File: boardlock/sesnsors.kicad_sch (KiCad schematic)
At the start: 1 part, among them U1 LSM6DS3

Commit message: update
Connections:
- net +3V3: now reaches U1.5 (VDDIO)
- net +3V3: now also U1.8 (VDD)
- net GND: now reaches U1.6 (GND), U1.7 (GND)
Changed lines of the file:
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@@
 (kicad_sch (version 20230121) (generator eeschema)
   (paper "A4")
+  (junction (at 81.28 44.45) (diameter 0) (color 0 0 0 0)
+  )
+  (wire (pts (xy 81.28 44.45) (xy 83.82 44.45))
+    (stroke (width 0) (type default))
+  )
+  (wire (pts (xy 81.28 81.28) (xy 81.28 86.36))
+    (stroke (width 0) (type default))
+  )
+  (wire (pts (xy 81.28 50.8) (xy 81.28 44.45))
+    (stroke (width 0) (type default))
+  )
+  (wire (pts (xy 83.82 50.8) (xy 83.82 44.45))
+    (stroke (width 0) (type default))
+  )
+  (wire (pts (xy 81.28 44.45) (xy 81.28 39.37))
+    (stroke (width 0) (type default))
+  )
   (symbol (lib_id "Sensor_Motion:LSM6DS3") (at 81.28 66.04 0) (unit 1)
     (in_bom yes) (on_board yes) (dnp no) (fields_autoplaced)
@@
         )
       )
+    )
+  )
+  (symbol (lib_id "power:+3V3") (at 81.28 39.37 0) (unit 1)
+    (in_bom yes) (on_board yes) (dnp no) (fields_autoplaced)
+    (property "Reference" "#PWR01" (at 81.28 43.18 0)
+      (effects (font (size 1.27 1.27)) hide)
+    )
+    (property "Value" "+3V3" (at 81.28 35.2369 0)
+      (effects (font (size 1.27 1.27)))
+    )
+    (property "Footprint" "" (at 81.28 39.37 0)
+      (effects (font (size 1.27 1.27)) hide)
+    )
+    (property "Datasheet" "" (at 81.28 39.37 0)
+      (effects (font (size 1.27 1.27)) hide)
+    )
+    (pin "1")
+    (instances
+      (project "boardlock"
+        (path "/48f24f42-fd64-4860-9f12-ca34cf195758/17b4aebf-aea4-4bb2-a07c-86de8cf47820"
+          (reference "#PWR01") (unit 1)
+        )
+      )
+    )
+  )
+  (symbol (lib_id "power:GND") (at 81.28 86.36 0) (unit 1)
+    (in_bom yes) (on_board yes) (dnp no) (fields_autoplaced)
+    (property "Reference" "#PWR02" (at 81.28 92.71 0)
+      (effects (font (size 1.27 1.27)) hide)
+    )
+    (property "Value" "GND" (at 81.28 90.4931 0)
+      (effects (font (size 1.27 1.27)))
+    )
+    (property "Footprint" "" (at 81.28 86.36 0)
+      (effects (font (size 1.27 1.27)) hide)
+    )
+    (property "Datasheet" "" (at 81.28 86.36 0)
+      (effects (font (size 1.27 1.27)) hide)
+    )
+    (pin "1")
+    (instances
+      (project "boardlock"
+        (path "/48f24f42-fd64-4860-9f12-ca34cf195758/17b4aebf-aea4-4bb2-a07c-86de8cf47820"
+          (reference "#PWR02") (unit 1)
+        )
+      )

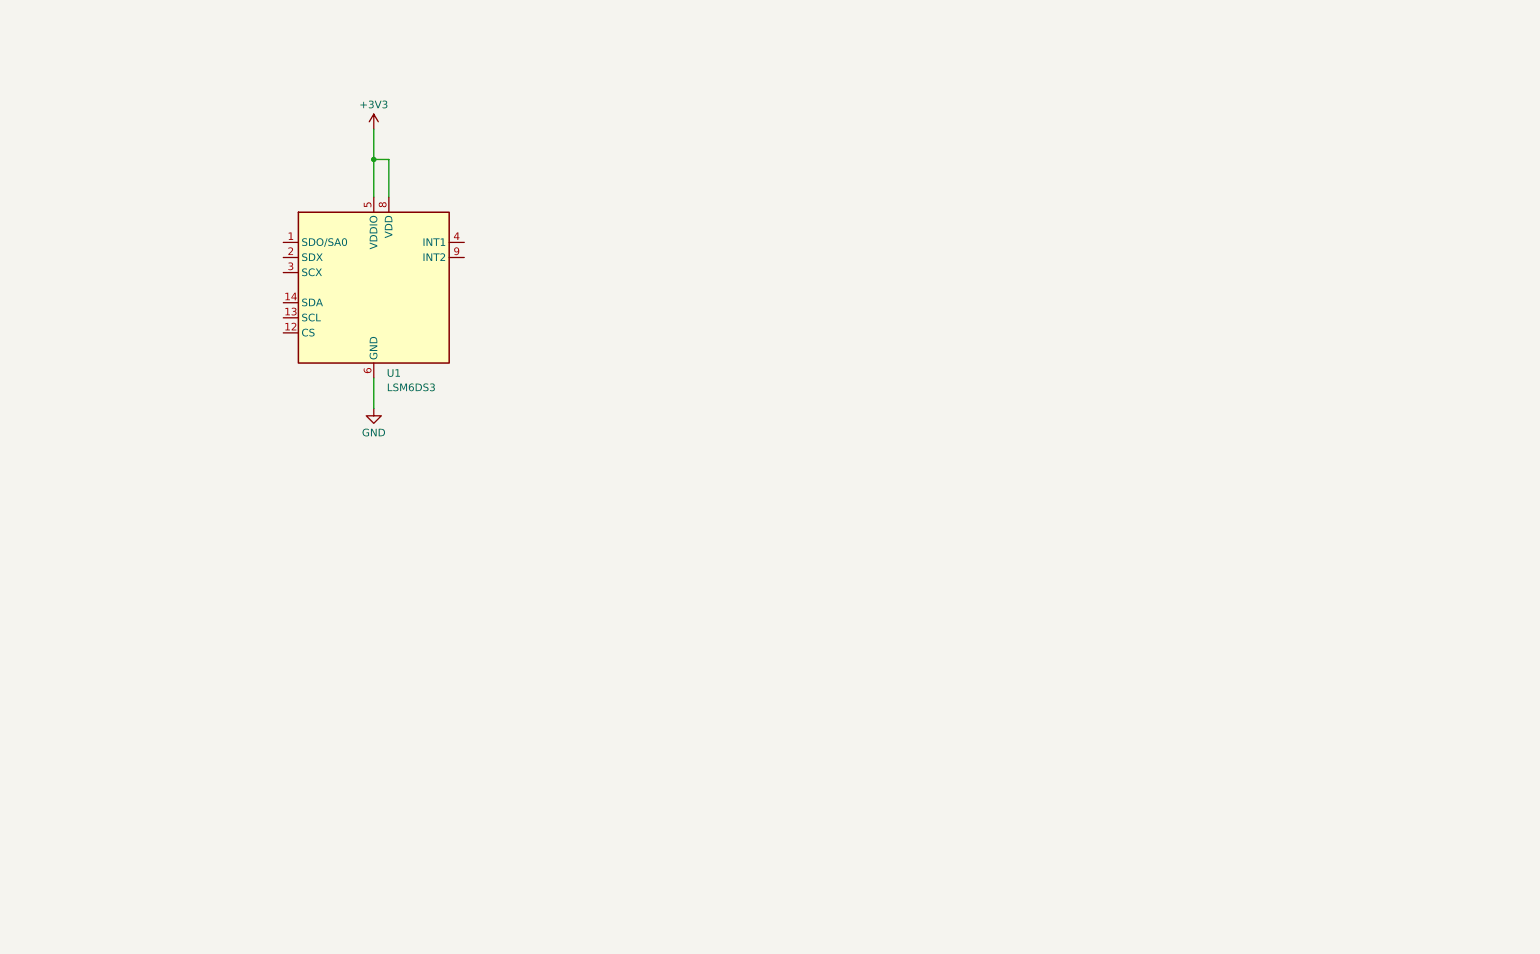
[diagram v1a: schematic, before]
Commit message: Started adding IMU and GPS circuits
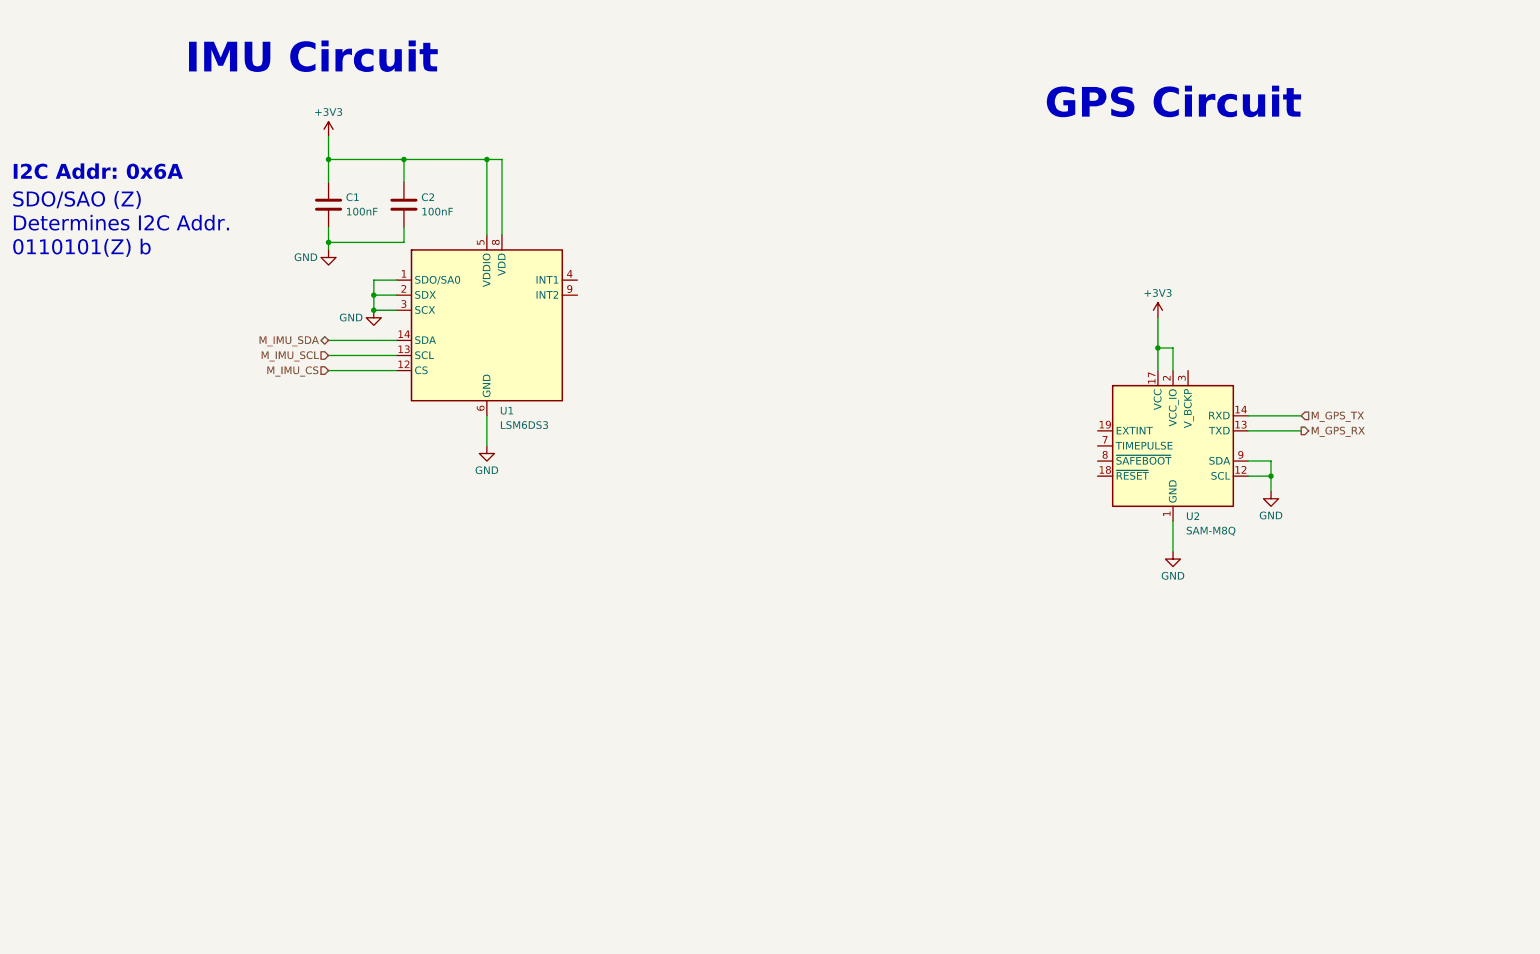
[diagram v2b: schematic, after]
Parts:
- added C1, C2: 100nF, symbol Device:C
- added U2: SAM-M8Q, RF_GPS:ublox_SAM-M8Q, symbol RF_GPS:SAM-M8Q
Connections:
- net +3V3: now also C1.1, C2.1, U2.17 (VCC), U2.2 (VCC_IO)
- net GND: now also U1.1 (SDO/SA0), U1.2 (SDX), U1.3 (SCX), C1.2, C2.2, U2.1 (GND), U2.10 (GND), U2.11 (GND), U2.12 (SCL), U2.15 (GND), U2.16 (GND), U2.20 (GND), U2.4 (GND), U2.5 (GND), U2.6 (GND), U2.9 (SDA)
- net M_IMU_CS: now reaches U1.12 (CS)
- net M_IMU_SCL: now reaches U1.13 (SCL)
- net M_IMU_SDA: now reaches U1.14 (SDA)
- new net M_GPS_RX: U2.13 (TXD)
- new net M_GPS_TX: U2.14 (RXD)
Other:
- note added: "GPS Circuit"
- note added: "I2C Addr: 0x6A"
- note added: "IMU Circuit"
- note added: "SDO/SAO (Z) Determines I2C Addr. 0110101(Z) b"
- moved on the sheet: U1

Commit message: updated GPS circuit
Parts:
- added Q1: Q_NMOS_GDS, symbol Device:Q_NMOS_GDS
- added R1, R2, R3, R4, R5, R6: R_US, symbol Device:R_US
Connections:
- net M_IMU_CS is gone; now on net GND: U1.12 (CS)
- net +3V3: now also R6.1; no longer U2.17 (VCC), U2.2 (VCC_IO)
- net GND: now also Q1.3 (S), R5.2; no longer U2.12 (SCL), U2.9 (SDA)
- net M_GPS_RX: now also R4.1; no longer U2.13 (TXD)
- net M_GPS_TX: now also R3.1; no longer U2.14 (RXD)
- net M_IMU_SCL: now also R2.1; no longer U1.13 (SCL)
- net M_IMU_SDA: now also R1.1; no longer U1.14 (SDA)
- new net: R2.2, U1.13 (SCL)
- new net: R1.2, U1.14 (SDA)
- new net: R4.2, U2.13 (TXD)
- new net: R3.2, U2.14 (RXD)
- new net GPS_POWER: Q1.2 (D), R6.2, U2.17 (VCC), U2.2 (VCC_IO)
- new net M_GPS_POWER: Q1.1 (G), R5.1
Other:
- note added: "EXTINT Leave open if not used."
- note added: "SDA, SCL leave open if not used."
- note added: "TIMEPULSE (Output) Configurable Timepulse signal (Default 1Hz). Leave open if not used."
- note added: "not sure about the V_backup since that's another battery our product needs..."
- note added: "~{RESET} Leave open if not used. Do not drive high. Do not connect a capacitor at this pin."
- note added: "~{SAFEBOOT} Leave open ."
- moved on the sheet: U2

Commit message: updates power control circuit
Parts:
- removed Q1: Q_NMOS_GDS, symbol Device:Q_NMOS_GDS
- removed R5, R6: R_US, symbol Device:R_US
- added Q1: Q_PMOS_GSD, symbol Device:Q_PMOS_GSD
- added Q2: Q_NPN_BCE, symbol Device:Q_NPN_BCE
- added R7, R8: R_US, symbol Device:R_US
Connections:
- net +3V3: now also Q1.2 (S), R7.1
- net GND: now also Q2.3 (E)
- net GPS_POWER: now also Q1.3 (D)
- net M_GPS_POWER: now also R8.1
- new net: Q1.1 (G), Q2.2 (C), R7.2
- new net: Q2.1 (B), R8.2
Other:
- note added: "GPS MAX Power Supply Current: 67mA"
- note added: "GPS Module"
- note added: "GPS Power Saving Circuit"
- moved on the sheet: R3, R4, U2

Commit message: update
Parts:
- added Q3: Q_NPN_BCE, symbol Device:Q_NPN_BCE
- added Q4: Q_PMOS_GSD, symbol Device:Q_PMOS_GSD
- added R5, R6: R_US, symbol Device:R_US
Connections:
- net +3V3: now also Q4.2 (S), R6.1; no longer C1.1, C2.1, U1.5 (VDDIO), U1.8 (VDD)
- net GND: now also Q3.3 (E)
- new net: Q3.1 (B), R5.2
- new net: Q3.2 (C), Q4.1 (G), R6.2
- new net IMU_POWER: C1.1, C2.1, Q4.3 (D), U1.5 (VDDIO), U1.8 (VDD)
- new net M_IMU_POWER: R5.1
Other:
- note added: "IMU Power Saving Circuit"
- moved on the sheet: C1, C2, Q1, Q2, R1, R2, R7, R8, U1

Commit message: updated comments
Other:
- note added: "Place each decoupling cap near VDD and VDDIO"
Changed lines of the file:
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@@
     (effects (font (size 1.27 1.27)) (justify left bottom))
+  )
+  (text "Place each decoupling cap\nnear VDD and VDDIO" (at 92.71 105.41 0)
+    (effects (font (size 1.27 1.27) bold) (justify left bottom))
   )
   (text "GPS Power Saving Circuit" (at 180.34 40.64 0)
@@
     (effects (font (size 5 5) (thickness 1) bold) (justify left bottom))
   )
-  (text "SDO/SAO (Z) \nDetermines I2C Addr.\n0110101(Z) b\n" (at 26.67 130.81 0)
+  (text "SDO/SAO (Z) \nDetermines I2C Addr.\n0110101(Z) b\n" (at 27.94 175.26 0)
     (effects (font (size 2.5 2.5)) (justify left bottom))
   )
@@
     (effects (font (size 1.27 1.27) bold) (justify left bottom))
   )
-  (text "I2C Addr: 0x6A" (at 26.67 118.11 0)
+  (text "I2C Addr: 0x6A" (at 27.94 162.56 0)
     (effects (font (size 2.5 2.5) (thickness 0.5) bold) (justify left bottom))
   )

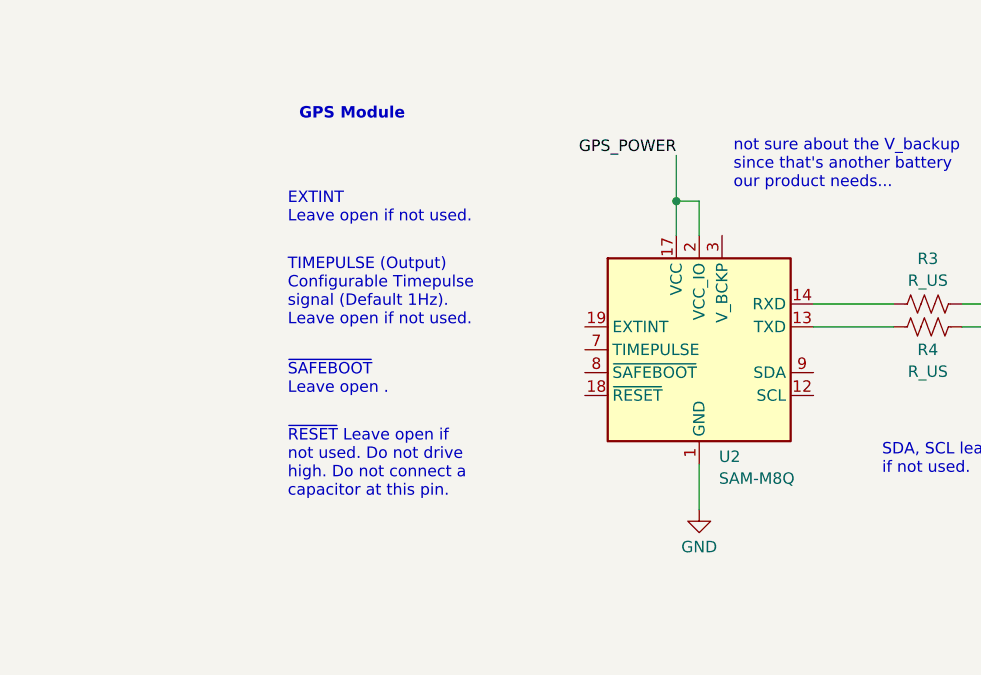
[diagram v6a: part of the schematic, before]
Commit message: small GPS changes and added .gitignore
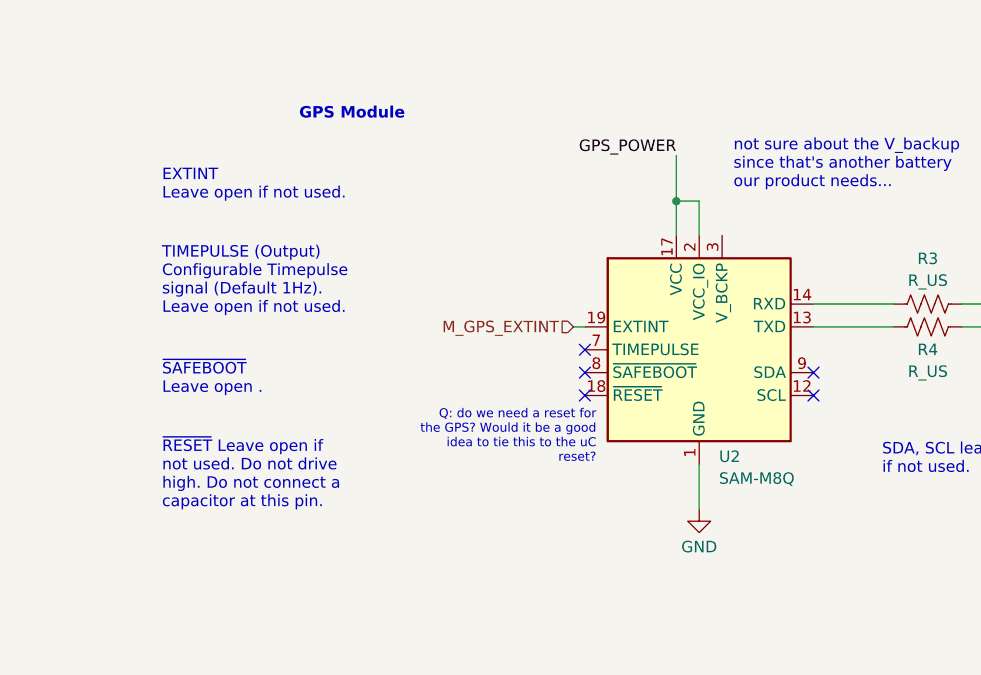
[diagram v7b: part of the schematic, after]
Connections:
- net M_GPS_EXTINT: now reaches U2.19 (EXTINT)
- no-connect marks 0 -> 5
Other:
- note added: "Q: do we need a reset for the GPS? Would it be a good idea to tie this to the uC reset?"
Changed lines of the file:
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@@
   (junction (at 87.63 137.16) (diameter 0) (color 0 0 0 0)
   )
+  (no_connect (at 208.28 125.73))
+  (no_connect (at 233.68 130.81))
+  (no_connect (at 208.28 130.81))
+  (no_connect (at 233.68 128.27))
+  (no_connect (at 208.28 128.27))
   (wire (pts (xy 64.77 60.96) (xy 64.77 63.5))
     (stroke (width 0) (type default))
@@
     (stroke (width 0) (type default))
   )
+  (wire (pts (xy 207.01 123.19) (xy 208.28 123.19))
+    (stroke (width 0) (type default))
+  )
   (wire (pts (xy 58.42 144.78) (xy 69.85 144.78))
     (stroke (width 0) (type default))
@@
   )
   (text "~{RESET} Leave open if\nnot used. Do not drive\nhigh. Do not connect a\ncapacitor at this pin."
-    (at 175.26 142.24 0)
+    (at 161.29 143.51 0)
     (effects (font (size 1.27 1.27)) (justify left bottom))
   )
   (text "Place each decoupling cap\nnear VDD and VDDIO" (at 92.71 105.41 0)
     (effects (font (size 1.27 1.27) bold) (justify left bottom))
+  )
+  (text "Q: do we need a reset for \nthe GPS? Would it be a good\nidea to tie this to the uC \nreset?"
+    (at 209.55 138.43 0)
+    (effects (font (size 1 1)) (justify right bottom))
   )
   (text "GPS Power Saving Circuit" (at 180.34 40.64 0)
@@
   )
   (text "TIMEPULSE (Output)\nConfigurable Timepulse\nsignal (Default 1Hz).\nLeave open if not used."
-    (at 175.26 123.19 0)
+    (at 161.29 121.92 0)
     (effects (font (size 1.27 1.27)) (justify left bottom))
   )
@@
     (effects (font (size 2.5 2.5)) (justify left bottom))
   )
-  (text "EXTINT\nLeave open if not used." (at 175.26 111.76 0)
+  (text "EXTINT\nLeave open if not used." (at 161.29 109.22 0)
     (effects (font (size 1.27 1.27)) (justify left bottom))
   )
@@
     (effects (font (size 2.5 2.5) (thickness 0.5) bold) (justify left bottom))
   )
-  (text "~{SAFEBOOT}\nLeave open ." (at 175.26 130.81 0)
+  (text "~{SAFEBOOT}\nLeave open ." (at 161.29 130.81 0)
     (effects (font (size 1.27 1.27)) (justify left bottom))
   )
@@
     (effects (font (size 1.27 1.27)) (justify right))
   )
+  (hierarchical_label "M_GPS_EXTINT" (shape input) (at 207.01 123.19 180) (fields_autoplaced)
+    (effects (font (size 1.27 1.27)) (justify right))
+  )
